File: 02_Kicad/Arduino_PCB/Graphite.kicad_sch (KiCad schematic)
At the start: 17 parts, among them J1 Power, J2 Digital/PWM, J3 Analog, J4 Digital/PWM, U1 LTC1050, U2 HC05

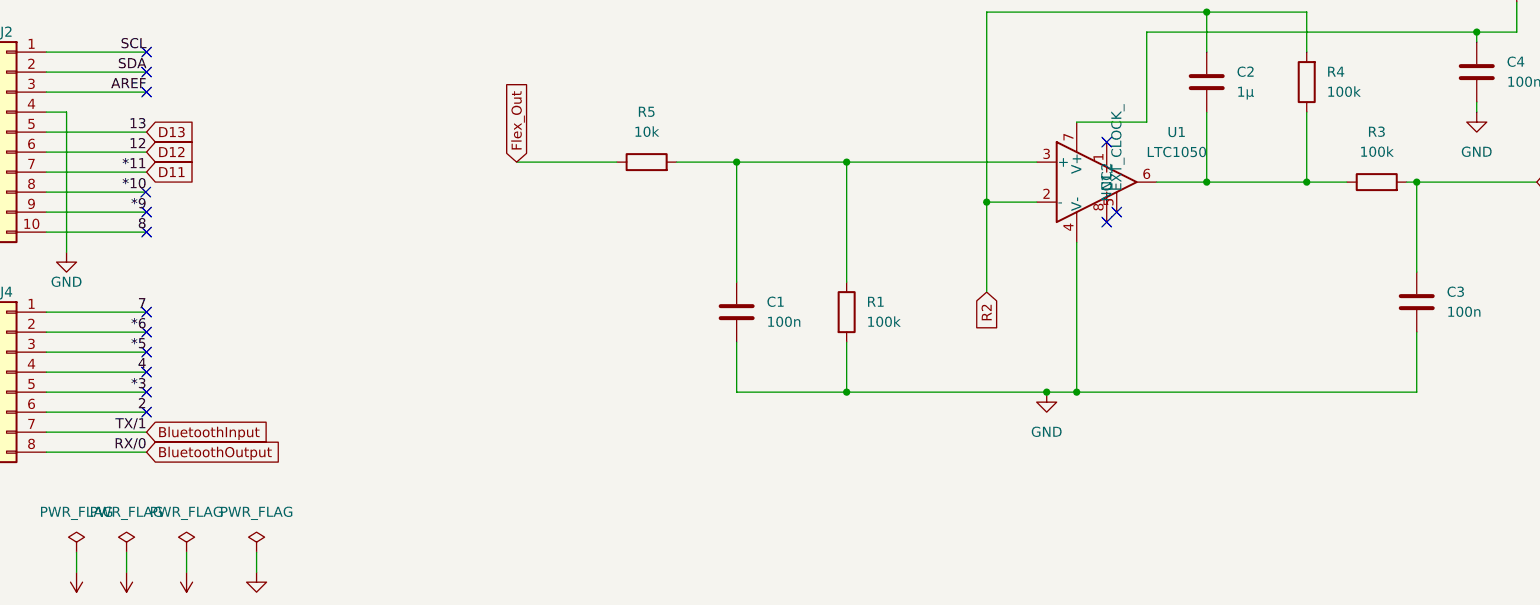
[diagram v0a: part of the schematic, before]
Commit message: Rectification Kicad
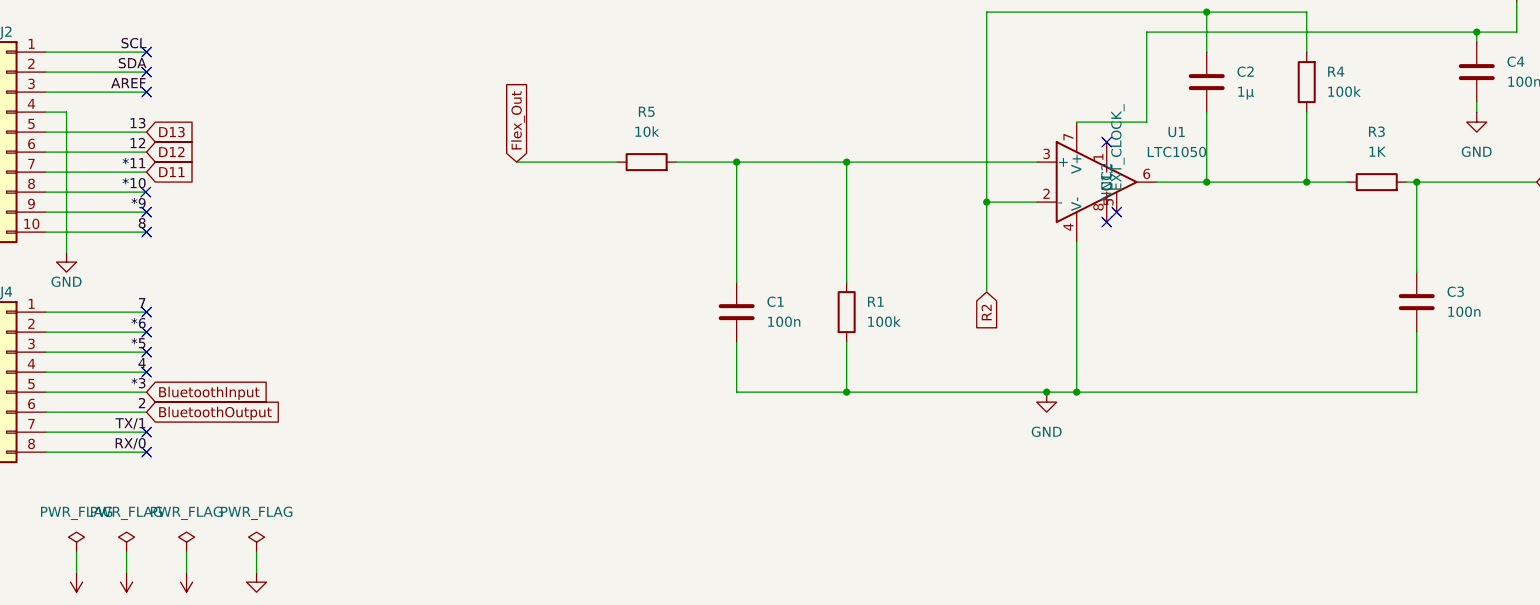
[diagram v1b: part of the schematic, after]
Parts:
- R3: value 100k -> 1K
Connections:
- net *3 is gone; now on net BluetoothInput: J4.5 (Pin_5)
- net 2 is gone; now on net BluetoothOutput: J4.6 (Pin_6)
- net BluetoothInput: no longer J4.7 (Pin_7)
- net BluetoothOutput: no longer J4.8 (Pin_8)
- new net RX/0: J4.8 (Pin_8)
- new net TX/1: J4.7 (Pin_7)
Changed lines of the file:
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@@
 	)
 	(no_connect
+		(at 74.93 74.93)
+	)
+	(no_connect
 		(at 74.93 31.75)
 	)
@@
 	)
 	(no_connect
-		(at 74.93 72.39)
+		(at 74.93 77.47)
 	)
 	(no_connect
@@
 		(at 21.59 67.31)
 	)
-	(no_connect
-		(at 74.93 69.85)
-	)
 	(wire
 		(pts
@@
 		)
 	)
-	(global_label "D12"
+	(global_label "BluetoothInput"
 		(shape input)
-		(at 74.93 39.37 0)
+		(at 74.93 69.85 0)
 		(fields_autoplaced yes)
 		(effects
@@
 		)
 		(property "Intersheetrefs" "${INTERSHEET_REFS}"
-			(at 81.6993 39.37 0)
+			(at 91.859 69.85 0)
 			(effects
 				(font
@@
 		)
 	)
-	(global_label "SCL"
+	(global_label "BluetoothOutput"
 		(shape input)
-		(at 21.59 72.39 180)
+		(at 74.93 72.39 0)
 		(fields_autoplaced yes)
 		(effects
@@
 				(size 1.27 1.27)
 			)
-			(justify right)
+			(justify left)
 		)
 		(property "Intersheetrefs" "${INTERSHEET_REFS}"
-			(at 15.0021 72.39 0)
+			(at 93.3104 72.39 0)
 			(effects
 				(font
 					(size 1.27 1.27)
 				)
-				(justify right)
+				(justify left)
 				(hide yes)
 			)
 		)
 	)
-	(global_label "SDA"
+	(global_label "D12"
 		(shape input)
-		(at 90.17 142.24 180)
+		(at 74.93 39.37 0)
 		(fields_autoplaced yes)
 		(effects
@@
 				(size 1.27 1.27)
 			)
-			(justify right)
+			(justify left)
 		)
 		(property "Intersheetrefs" "${INTERSHEET_REFS}"
-			(at 83.5216 142.24 0)
+			(at 81.6993 39.37 0)
 			(effects
 				(font
 					(size 1.27 1.27)
 				)
-				(justify right)
+				(justify left)
 				(hide yes)
 			)
 		)
 	)
-	(global_label "AmpliOut"
+	(global_label "SCL"
 		(shape input)
-		(at 24.13 62.23 180)
+		(at 21.59 72.39 180)
 		(fields_autoplaced yes)
 		(effects
@@
 		)
 		(property "Intersheetrefs" "${INTERSHEET_REFS}"
-			(at 12.6436 62.23 0)
+			(at 15.0021 72.39 0)
 			(effects
 				(font
@@
 		)
 	)
-	(global_label "BluetoothInput"
+	(global_label "SDA"
 		(shape input)
-		(at 149.86 147.32 180)
+		(at 90.17 142.24 180)
 		(fields_autoplaced yes)
 		(effects
@@
 		)
 		(property "Intersheetrefs" "${INTERSHEET_REFS}"
-			(at 132.931 147.32 0)
+			(at 83.5216 142.24 0)
 			(effects
 				(font
@@
 		)
 	)
-	(global_label "BluetoothInput"
+	(global_label "AmpliOut"
 		(shape input)
-		(at 74.93 74.93 0)
+		(at 24.13 62.23 180)
 		(fields_autoplaced yes)
 		(effects
@@
 				(size 1.27 1.27)
 			)
-			(justify left)
+			(justify right)
 		)
 		(property "Intersheetrefs" "${INTERSHEET_REFS}"
-			(at 91.859 74.93 0)
+			(at 12.6436 62.23 0)
 			(effects
 				(font
 					(size 1.27 1.27)
 				)
-				(justify left)
+				(justify right)
 				(hide yes)
 			)
 		)
 	)
-	(global_label "SCL"
+	(global_label "BluetoothInput"
 		(shape input)
-		(at 90.17 139.7 180)
+		(at 149.86 147.32 180)
 		(fields_autoplaced yes)
 		(effects
@@
 		)
 		(property "Intersheetrefs" "${INTERSHEET_REFS}"
-			(at 83.5821 139.7 0)
+			(at 132.931 147.32 0)
 			(effects
 				(font
@@
 		)
 	)
-	(global_label "BluetoothOutput"
+	(global_label "SCL"
 		(shape input)
-		(at 74.93 77.47 0)
+		(at 90.17 139.7 180)
 		(fields_autoplaced yes)
 		(effects
@@
 				(size 1.27 1.27)
 			)
-			(justify left)
+			(justify right)
 		)
 		(property "Intersheetrefs" "${INTERSHEET_REFS}"
-			(at 93.3104 77.47 0)
+			(at 83.5821 139.7 0)
 			(effects
 				(font
 					(size 1.27 1.27)
 				)
-				(justify left)
+				(justify right)
 				(hide yes)
 			)
@@
 			)
 		)
-		(property "Value" "100k"
+		(property "Value" "1K"
 			(at 231.14 39.37 90)
 			(effects
